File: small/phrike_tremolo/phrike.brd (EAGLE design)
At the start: 33 x 41.9 mm, 38 parts, among them Q1 2N5457, Q2 2N3904, Q3 2N5457, Q4 2N5088

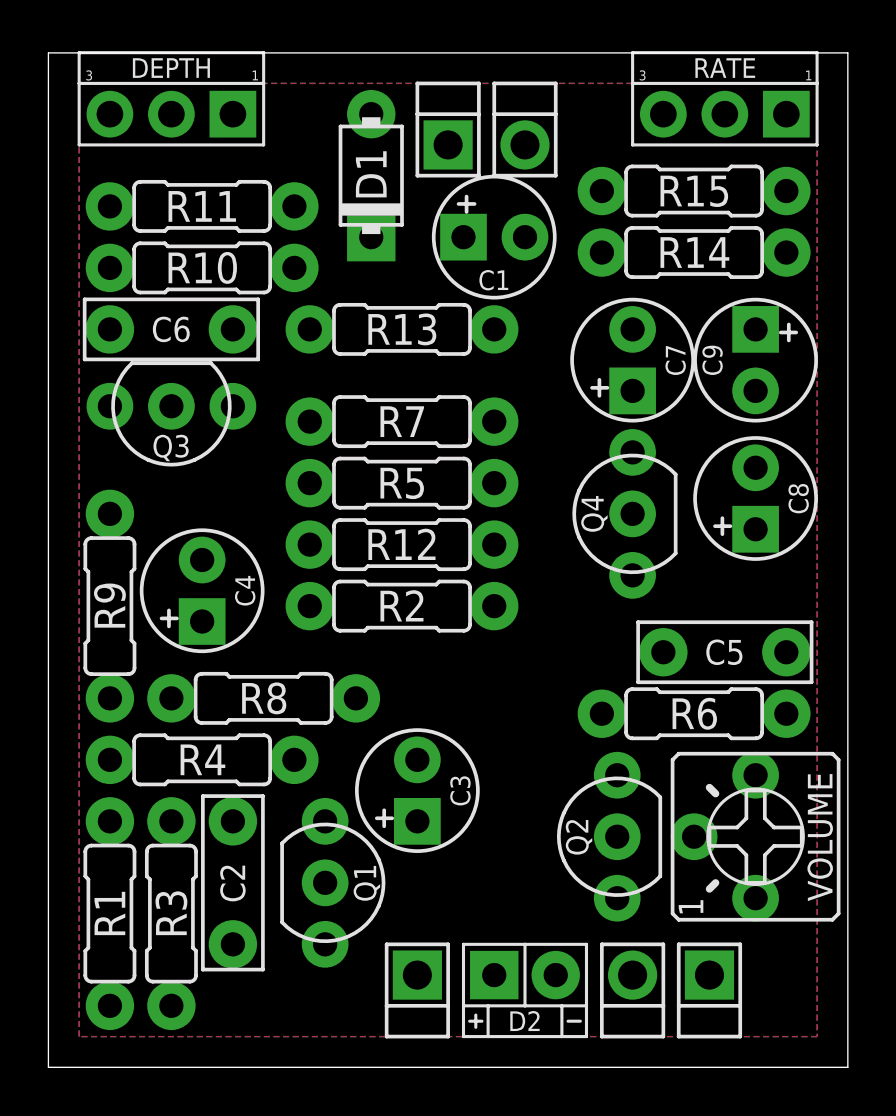
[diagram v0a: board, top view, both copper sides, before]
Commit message: add EAGLE library, update 1590a chorus and tremolo, other minor edits
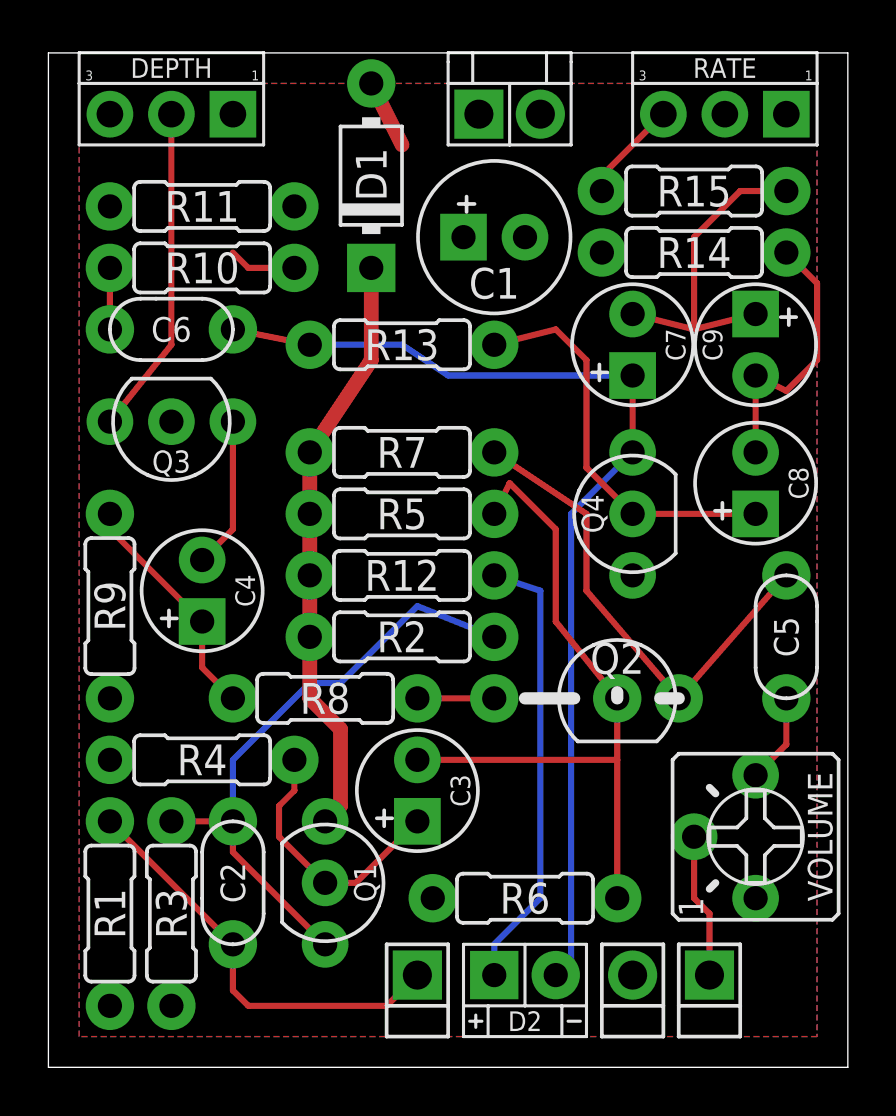
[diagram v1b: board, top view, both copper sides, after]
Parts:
- removed PAD1: PADSQR, supply pins:SQUARE
- removed PAD4: PADRND, supply pins:ROUND
- added 9V: DC_MONO, jacks:DC
- C1: device capacitors-elec:050_020_1 -> capacitors-elec:063_025
- C2: value 47n/100n -> 47n; device capacitors-film:BOX_SMALL -> capacitors-film:050X030_025_2
- C4: value 22u/10u -> 22u
- C5, C6: value 47n/10u -> 47n; device capacitors-film:BOX_SMALL -> capacitors-film:050X030_025_2
- C8, C9: value 1u/470n -> 1u
- D1: value 2N4001 -> 2N5417; device diodes:DO41-2 -> diodes:DO41-3
- DEPTH: value 250kB/1MB -> 1MB
- Q2: device transistors:TO92- -> transistors:TO92-L2
- R1: value 1M/470k -> 1M
- R10: value 120k/100k -> 100k
- R11: value 68k/x -> 560k
- R9: value 1k2 (2k2) -> 1k2
- VOLUME: value 25k (100k) -> 25k
- moved R6 10.3 mm to (19.7, 6.99), turned to 0 degrees
- moved Q2 5.71 mm to (23.5, 15.2), turned to 0 degrees
- moved C5 2.62 mm to (30.5, 17.8), turned to 90 degrees
- moved R8 2.54 mm to (11.4, 15.2)
- moved R7 1.27 mm to (14.6, 25.4)
- moved R12 1.27 mm to (14.6, 20.3)
- moved R2 1.27 mm to (14.6, 17.8)
- moved R5 1.27 mm to (14.6, 22.9)
- moved R13 0.64 mm to (14.6, 29.8)
- moved C7 0.63 mm to (24.1, 29.8)
- moved C8 0.63 mm to (29.2, 24.1)
- moved C9 0.63 mm to (29.2, 29.8)
- moved Q3 0.63 mm to (5.08, 26.7)
- turned R11 to 0 degrees
- renumbered PAD2 to IN, PAD3 to OUT, PAD5 to GND
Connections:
- net +9V: now also 9V.T; no longer PAD1.1
- net GND: now also 9V.S; no longer PAD4.1
- net N$11: now also DEPTH.3; no longer DEPTH.1
- net N$17: now also DEPTH.1; no longer DEPTH.3
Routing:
- net N$13: track 0.00 -> 43.0 mm
- net N$3: track 0.00 -> 28.5 mm
- net N$1: track 0.00 -> 25.4 mm
- net N$7: track 0.00 -> 24.4 mm
- net N$4: track 0.00 -> 20.4 mm
- net N$19: track 0.00 -> 18.7 mm
- net IN: track 0.00 -> 17.5 mm
- net N$14: track 0.00 -> 16.6 mm
- net N$15: track 0.00 -> 13.6 mm
- net N$10: track 0.00 -> 13.6 mm
- net N$16: track 0.00 -> 11.4 mm
- net N$2: track 0.00 -> 11.0 mm
- net N$8: track 0.00 -> 9.72 mm
- net N$9: track 0.00 -> 6.24 mm
- net OUT: track 0.00 -> 5.98 mm
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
